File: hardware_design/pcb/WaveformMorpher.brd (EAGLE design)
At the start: 128.8 x 106.5 mm, 67 parts, among them IC1 MAX11615EEE+, IC2 TL074D, IC3 LM4041B12DBZ, IC4 LME49720MAX_NOPB, J1 GATE_J, J2 MORPH_J, J3 1V/OCT_J, J4 LOOP_J, J5 RASP_IN_J, J6 OUT_J, T1 MMBT3904

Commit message: Board first placements
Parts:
- moved R26 210.3 mm to (127.0, 47.0), turned to 90 degrees
- moved R24 202.2 mm to (118.1, 20.3), turned to 270 degrees
- moved R7 196.5 mm to (120.7, 24.1), turned to 90 degrees
- moved R6 186.3 mm to (121.9, 53.3), turned to 90 degrees
- moved J5 185.6 mm to (120.7, 43.2)
- moved IC4 181.5 mm to (108.0, 16.5), turned to 180 degrees
- moved R5 178.3 mm to (120.7, 68.6), turned to 90 degrees
- moved R4 174.1 mm to (121.9, 86.4), turned to 90 degrees
- moved C1 170.2 mm to (88.9, 59.7)
- moved C12 167.1 mm to (111.8, 22.9), turned to 270 degrees
- moved C6 165.2 mm to (127.0, 35.6), turned to 90 degrees
- moved R8 165.1 mm to (97.8, 55.9)
- moved R9 163.8 mm to (91.4, 55.9)
- moved R27 159.3 mm to (127.0, 39.4), turned to 90 degrees
- moved C11 157.8 mm to (104.1, 11.4), turned to 270 degrees
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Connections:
- removed net 1V/OCT_ADC1: C3.2, R18.2
- net MORPH_ADC: now also C3.2, R18.2

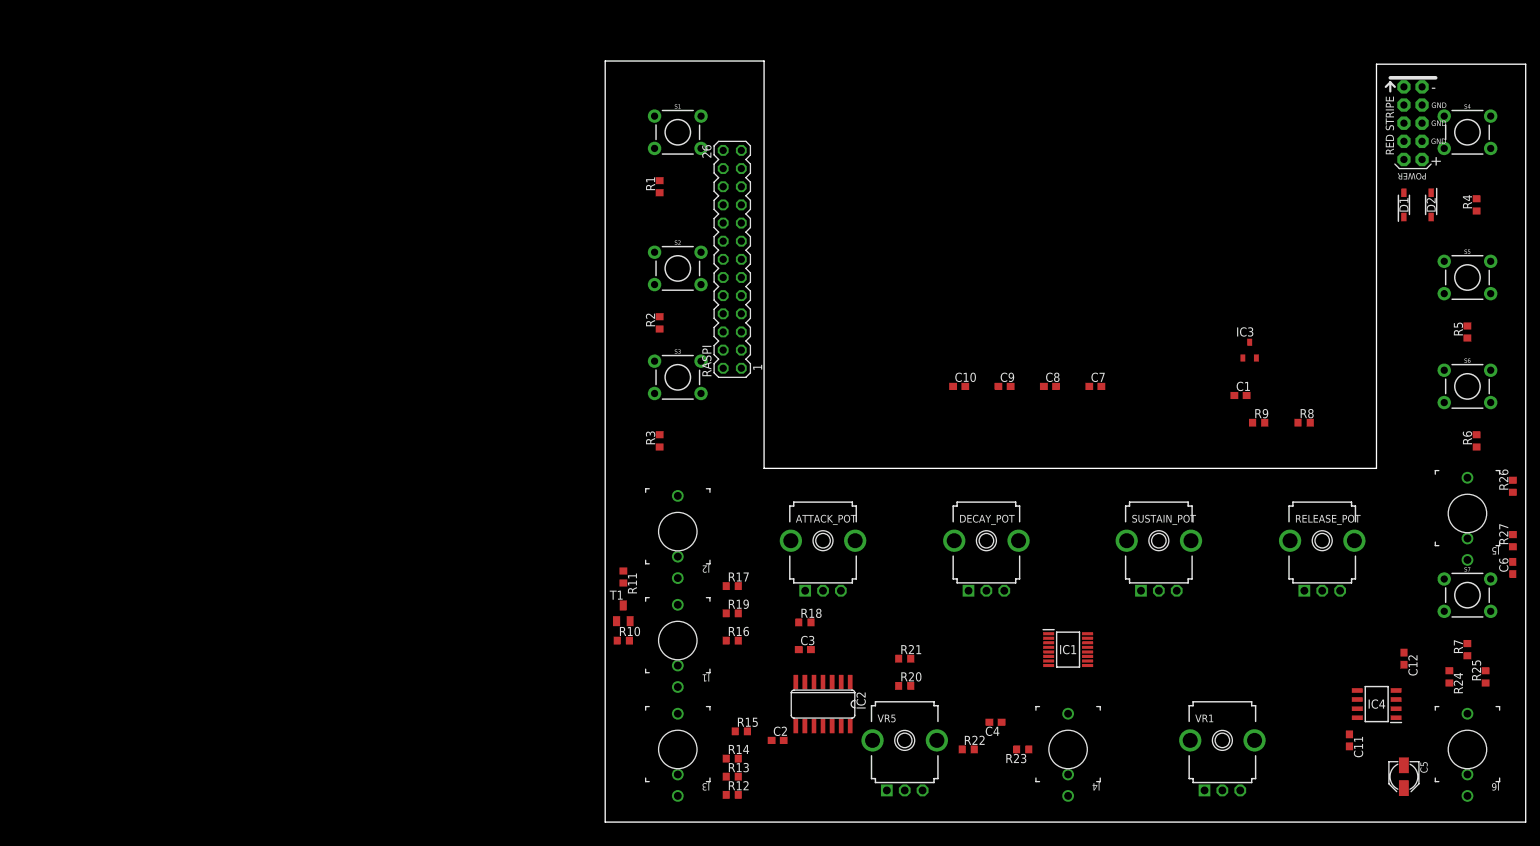
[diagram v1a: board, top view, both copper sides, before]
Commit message: adding vias
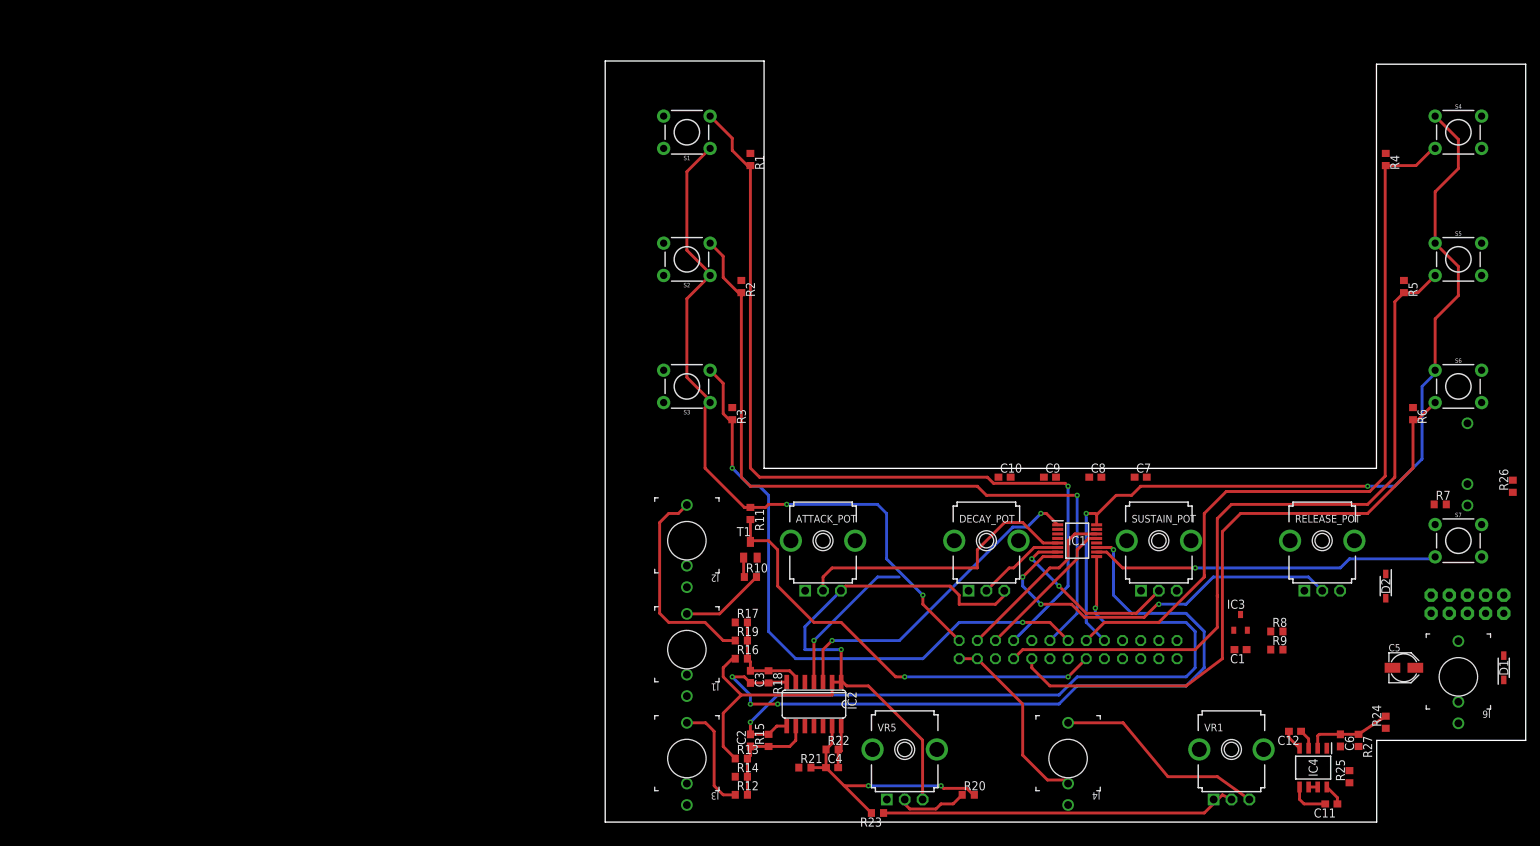
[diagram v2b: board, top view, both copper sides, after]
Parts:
- moved RASPI 72.0 mm to (64.8, 24.1), flipped to the bottom, turned to 180 degrees
- moved JP1 67.7 mm to (120.7, 30.5), flipped to the bottom, turned to 0 degrees
- moved D1 66.3 mm to (125.7, 21.6)
- moved D2 53.7 mm to (109.2, 33.0)
- moved IC3 38.1 mm to (88.9, 27.9)
- moved C1 35.6 mm to (88.9, 24.1), turned to 180 degrees
- moved R27 35.3 mm to (105.4, 11.4), turned to 270 degrees
- moved C6 34.1 mm to (102.9, 11.4), turned to 270 degrees
- moved R9 31.9 mm to (94.0, 24.1)
- moved R8 29.5 mm to (94.0, 26.7)
- moved C4 23.7 mm to (31.8, 7.62), turned to 0 degrees
- moved R25 23.6 mm to (104.1, 6.35)
- moved R23 22.2 mm to (38.1, 1.27)
- moved R7 20.7 mm to (116.8, 44.5), turned to 0 degrees
- moved R21 20.7 mm to (27.9, 7.62)
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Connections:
- removed net N$13: IC2.9, R19.2
- net 1V/OCT_ADC: now also IC2.8; no longer IC2.7
- net GND: now also J2.P$3_SLEEVE, J3.P$3_SLEEVE; no longer J2.P$1_TIP, J2.P$2_SWITCH, J3.P$1_TIP, J3.P$2_SWITCH
- net MORPH_ADC: now also IC2.7; no longer IC2.8
- net N$10: now also IC2.6, R19.2
- net N$12: now also J3.P$1_TIP, R12.1; no longer J2.P$3_SLEEVE, R19.1
- net N$8: now also J2.P$1_TIP, R19.1; no longer J3.P$3_SLEEVE, R12.1
- net N$9: now also IC2.9; no longer IC2.6
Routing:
- net 3.3V: track 0.00 -> 225.4 mm, vias 0 -> 4
- net SW1_GPIO: track 0.00 -> 122.1 mm, vias 0 -> 1
- net SW4_GPIO: track 0.00 -> 108.0 mm
- net MORPH_ADC: track 0.00 -> 107.2 mm, vias 0 -> 4
- net SW2_GPIO: track 0.00 -> 104.9 mm, vias 0 -> 1
- net SW5_GPIO: track 0.00 -> 104.7 mm
- net VREF2.0: track 0.00 -> 102.3 mm, vias 0 -> 1
- net 1V/OCT_ADC: track 0.00 -> 100.8 mm, vias 0 -> 2
- net SW6_GPIO: track 0.00 -> 89.3 mm
- net SW3_GPIO: track 0.00 -> 87.6 mm, vias 0 -> 2
- net GATE_ADC: track 0.00 -> 62.1 mm, vias 0 -> 2
- net RELEASE_ADC: track 0.00 -> 54.2 mm, vias 0 -> 3
- net N$24: track 0.00 -> 49.9 mm
- net SW7_GPIO: track 0.00 -> 48.9 mm, vias 0 -> 1
- net N$3: track 0.00 -> 45.9 mm, vias 0 -> 2
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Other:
- outline, holes or cut-outs redrawn

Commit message: finishing up the board
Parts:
- removed C7, C9: 100n, rcl:C0603
- P1, P2, P3, P4: value (none) -> 10kB
- P5: value LOOP_POT -> 10kB
- P6: value LOOP_CV_POT -> 10kB
- moved C10 22.6 mm to (41.9, 30.5), turned to 180 degrees
- moved R7 10.2 mm to (108.0, 39.4), turned to 270 degrees
- moved D2 9.92 mm to (101.6, 26.7), turned to 180 degrees
- moved R25 8.98 mm to (102.9, 15.2)
- moved R26 6.35 mm to (127.0, 53.3)
- moved R24 4.02 mm to (105.4, 15.2), turned to 270 degrees
- moved R4 2.84 mm to (111.8, 91.4), turned to 90 degrees
- moved C8 2.54 mm to (68.6, 45.7), turned to 90 degrees
- moved C1 2.54 mm to (91.4, 24.1)
- moved IC3 2.54 mm to (91.4, 27.9)
- moved C5 1.27 mm to (110.5, 21.6)
- moved R8 1.27 mm to (95.2, 26.7)
- moved R9 1.27 mm to (95.2, 24.1)
- turned JP1 to 180 degrees
- renumbered ATTACK_POT to P1, DECAY_POT to P2, RELEASE_POT to P4, SUSTAIN_POT to P3, VR1 to P6, VR5 to P5
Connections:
- removed net N$2: C10.1, C7.1, C8.1, C9.1
- removed net V+: IC2.4
- removed net V-: IC2.11
- net 3.3V: now also C10.1, C8.1, IC2.4
- net GND: now also IC2.11; no longer C7.2, C9.2
- net N$11: now also D1.2, JP1.10; no longer D2.1
- net N$7: now also D2.1, JP1.2; no longer D1.2
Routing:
- net VREF2.0: track 102.3 -> 241.6 mm, vias 1 -> 2
- net -10V: track 0.00 -> 135.9 mm, vias 0 -> 4
- net LOOP_ADC: track 6.45 -> 106.5 mm, vias 0 -> 4
- net GND: track 8.40 -> 89.1 mm, vias 0 -> 10
- net N$18: track 0.00 -> 78.6 mm, vias 0 -> 2
- net 3.3V: track 225.4 -> 290.7 mm, vias 4 -> 7
- net +12V: track 2.98 -> 37.4 mm
- net V+: track 21.4 -> 0.00 mm, vias 1 -> 0
- net -12V: track 2.98 -> 21.8 mm
- net N$7: track 0.00 -> 15.9 mm
- net N$21: track 0.00 -> 10.8 mm
- net N$20: track 0.00 -> 8.84 mm
- net N$11: track 0.00 -> 8.46 mm
- net N$19: track 0.00 -> 7.02 mm
- net SW2_GPIO: track 104.9 -> 107.7 mm
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- added copper zone on layer 1, net GND
- added copper zone on layer 16, net GND

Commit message: hardware v0.7
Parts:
- IC2: value TL074D -> MCP6004
- moved R1 3.59 mm to (17.8, 90.2), turned to 90 degrees
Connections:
- net GATE_ADC renamed GATE_GPIO
- net SW7_GPIO renamed SW7_ADC
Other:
- outline, holes or cut-outs redrawn

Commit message: partlist and bugfixes
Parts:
- IC3: value LM4041B12DBZ -> LM4040B10
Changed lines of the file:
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@@
 </element>
 <element name="IC2" library="gm-ics" package="SO14" value="MCP6004" x="29.21" y="16.51" rot="R180"/>
-<element name="IC3" library="texas" package="DBZ_R-PDSO-G3" value="LM4041B12DBZ" x="91.44" y="27.94">
+<element name="IC3" library="texas" package="DBZ_R-PDSO-G3" value="LM4040B10" x="91.44" y="27.94">
 <attribute name="MF" value="" x="91.44" y="27.94" size="1.778" layer="27" display="off"/>
 <attribute name="MPN" value="LM4041B12IDBZR" x="91.44" y="27.94" size="1.778" layer="27" display="off"/>
